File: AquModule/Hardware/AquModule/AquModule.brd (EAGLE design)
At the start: 160 x 100 mm, 1 part

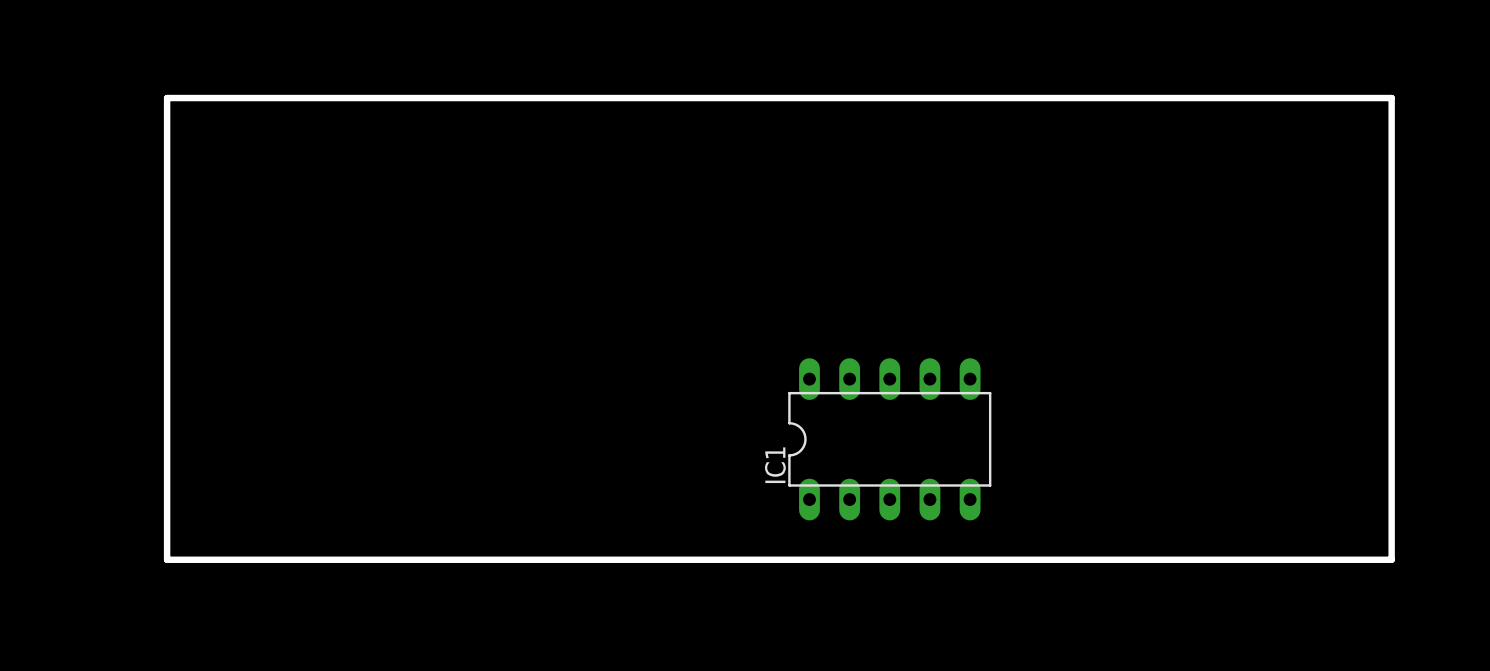
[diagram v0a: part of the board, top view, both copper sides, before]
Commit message: Wired all the components and made first PCB wiring
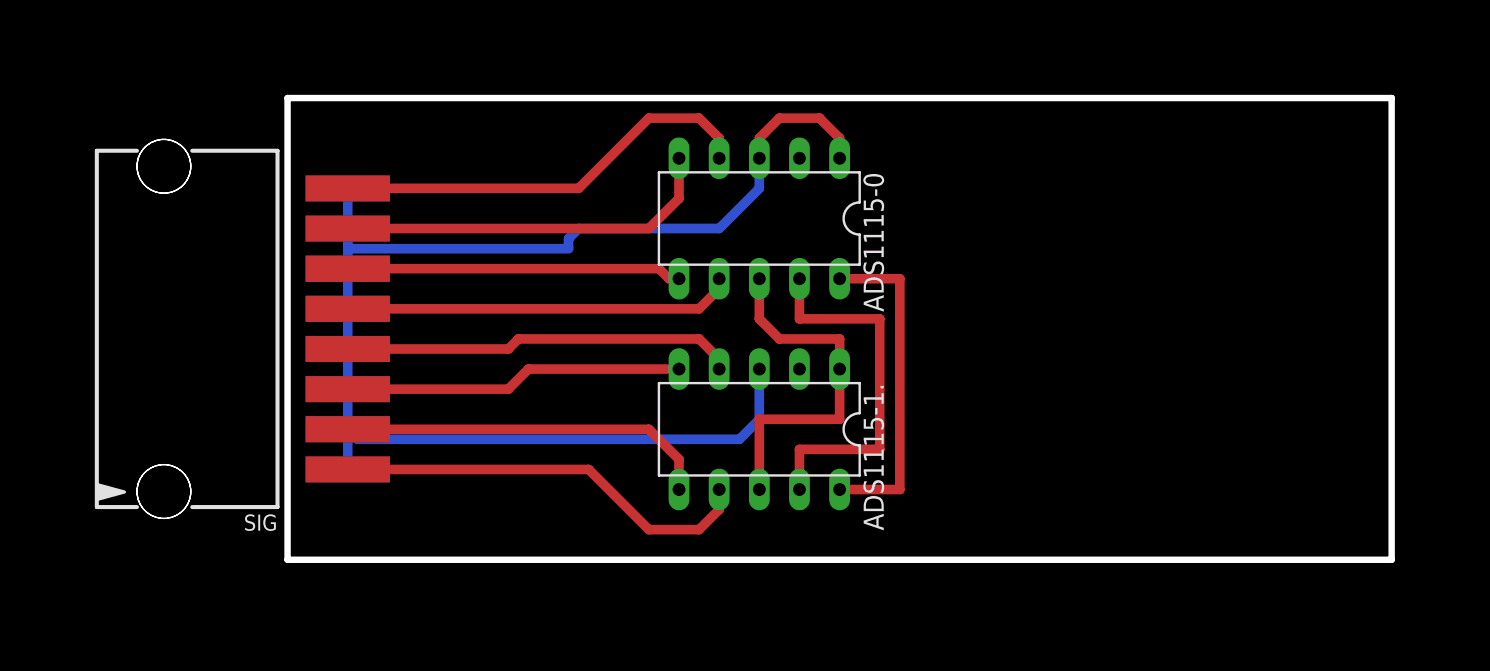
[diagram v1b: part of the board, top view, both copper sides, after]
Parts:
- removed IC1: (no value), ic-package:DIL10
- added ADS1115-0, ADS1115-1.: (no value), ic-package:DIL10
- added GND: GND, con-molex:15-91-08
- added SIG: SIG, con-molex:15-91-08
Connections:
- new net GND: ADS1115-0.1, ADS1115-0.3, ADS1115-1..3, GND.1, GND.2, GND.3, GND.4, GND.5, GND.6, GND.7, GND.8
- new net N$1: ADS1115-0.4, SIG.8
- new net N$2: ADS1115-0.5, SIG.7
- new net N$3: ADS1115-0.6, SIG.6
- new net N$4: ADS1115-0.7, SIG.5
- new net N$5: ADS1115-1..4, SIG.4
- new net N$6: ADS1115-1..5, SIG.3
- new net N$7: ADS1115-1..6, SIG.2
- new net N$8: ADS1115-1..7, SIG.1
- new net SCL: ADS1115-0.10, ADS1115-1..10
- new net SDA: ADS1115-0.9, ADS1115-1..9
- new net VCC: ADS1115-0.8, ADS1115-1..1, ADS1115-1..8
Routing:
- net GND: track 0.00 -> 86.3 mm
- net N$1: track 0.00 -> 27.1 mm
- net N$8: track 0.00 -> 26.9 mm
- net N$5: track 0.00 -> 24.9 mm
- net N$4: track 0.00 -> 24.7 mm
- net N$2: track 0.00 -> 24.3 mm
- net N$7: track 0.00 -> 23.6 mm
- net SDA: track 0.00 -> 23.5 mm
- net VCC: track 0.00 -> 22.8 mm
- net N$6: track 0.00 -> 21.5 mm
- net N$3: track 0.00 -> 21.2 mm
- net SCL: track 0.00 -> 21.0 mm
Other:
- outline, holes or cut-outs redrawn
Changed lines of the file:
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@@
 <setting verticaltext="up"/>
 </settings>
-<grid distance="0.05" unitdist="inch" unit="mm" style="dots" multiple="1" display="yes" altdistance="0.025" altunitdist="inch" altunit="inch"/>
+<grid distance="0.635" unitdist="mm" unit="mm" style="dots" multiple="1" display="yes" altdistance="0.025" altunitdist="inch" altunit="inch"/>
 <layers>
 <layer number="1" name="Top" color="4" fill="1" visible="yes" active="yes"/>
@@
 <dimension x1="38.1" y1="71.12" x2="115.57" y2="71.12" x3="76.835" y3="77.47" textsize="1.778" layer="46"/>
 <dimension x1="115.57" y1="71.12" x2="115.57" y2="41.91" x3="121.92" y3="56.515" textsize="1.778" layer="46"/>
-<wire x1="38.1" y1="71.12" x2="115.57" y2="71.12" width="0.4064" layer="46"/>
+<wire x1="45.72" y1="71.12" x2="115.57" y2="71.12" width="0.4064" layer="46"/>
 <wire x1="115.57" y1="71.12" x2="115.57" y2="41.91" width="0.4064" layer="46"/>
-<wire x1="115.57" y1="41.91" x2="38.1" y2="41.91" width="0.4064" layer="46"/>
-<wire x1="38.1" y1="41.91" x2="38.1" y2="71.12" width="0.4064" layer="46"/>
+<wire x1="115.57" y1="41.91" x2="45.72" y2="41.91" width="0.4064" layer="46"/>
+<wire x1="45.72" y1="41.91" x2="45.72" y2="71.12" width="0.4064" layer="46"/>
 </plain>
 <attributes>
@@
 </autorouter>
 <elements>
-<element name="IC1" library="ic-package" package="DIL10" value="" x="83.82" y="49.53"/>
+<element name="ADS1115-1." library="ic-package" package="DIL10" value="" x="75.565" y="50.165" rot="R180"/>
+<element name="SIG" library="con-molex" package="15-91-08" value="SIG" x="38.735" y="56.515" rot="R90">
+<attribute name="OC_NEWARK" value="unknown" x="38.735" y="56.515" size="1.778" layer="27" rot="R90" display="off"/>
+<attribute name="MPN" value="" x="38.735" y="56.515" size="1.778" layer="27" rot="R90" display="off"/>
+<attribute name="MF" value="" x="38.735" y="56.515" size="1.778" layer="27" rot="R90" display="off"/>
+<attribute name="OC_FARNELL" value="unknown" x="38.735" y="56.515" size="1.778" layer="27" rot="R90" display="off"/>
+</element>
+<element name="GND" library="con-molex" package="15-91-08" value="GND" x="38.735" y="56.515" rot="MR270">
+<attribute name="OC_NEWARK" value="unknown" x="38.735" y="56.515" size="1.778" layer="28" rot="MR270" display="off"/>
+<attribute name="MPN" value="" x="38.735" y="56.515" size="1.778" layer="28" rot="MR270" display="off"/>
+<attribute name="MF" value="" x="38.735" y="56.515" size="1.778" layer="28" rot="MR270" display="off"/>
+<attribute name="OC_FARNELL" value="unknown" x="38.735" y="56.515" size="1.778" layer="28" rot="MR270" display="off"/>
+</element>
+<element name="ADS1115-0" library="ic-package" package="DIL10" value="" x="75.565" y="63.5" rot="R180"/>
 </elements>
 <signals>
+<signal name="N$1">
+<contactref element="ADS1115-0" pad="4"/>
+<contactref element="SIG" pad="8"/>
+<wire x1="73.025" y1="67.31" x2="73.025" y2="68.58" width="0.6096" layer="1"/>
+<wire x1="73.025" y1="68.58" x2="71.755" y2="69.85" width="0.6096" layer="1"/>
+<wire x1="71.755" y1="69.85" x2="68.58" y2="69.85" width="0.6096" layer="1"/>
+<wire x1="68.58" y1="69.85" x2="64.135" y2="65.405" width="0.6096" layer="1"/>
+<wire x1="64.135" y1="65.405" x2="49.53" y2="65.405" width="0.6096" layer="1"/>
+</signal>
+<signal name="N$2">
+<contactref element="ADS1115-0" pad="5"/>
+<contactref element="SIG" pad="7"/>
+<wire x1="49.53" y1="62.865" x2="68.58" y2="62.865" width="0.6096" layer="1"/>
+<wire x1="68.58" y1="62.865" x2="70.485" y2="64.77" width="0.6096" layer="1"/>
+<wire x1="70.485" y1="64.77" x2="70.485" y2="67.31" width="0.6096" layer="1"/>
+</signal>
+<signal name="N$3">
+<contactref element="ADS1115-0" pad="6"/>
+<contactref element="SIG" pad="6"/>
+<wire x1="70.485" y1="59.69" x2="69.85" y2="59.69" width="0.6096" layer="1"/>
+<wire x1="69.85" y1="59.69" x2="69.215" y2="60.325" width="0.6096" layer="1"/>
+<wire x1="69.215" y1="60.325" x2="49.53" y2="60.325" width="0.6096" layer="1"/>
+</signal>
+<signal name="N$4">
+<contactref element="ADS1115-0" pad="7"/>
+<contactref element="SIG" pad="5"/>
+<wire x1="49.53" y1="57.785" x2="71.755" y2="57.785" width="0.6096" layer="1"/>
+<wire x1="71.755" y1="57.785" x2="73.025" y2="59.055" width="0.6096" layer="1"/>
+<wire x1="73.025" y1="59.055" x2="73.025" y2="59.69" width="0.6096" layer="1"/>
+</signal>
+<signal name="N$5">
+<contactref element="ADS1115-1." pad="4"/>
+<contactref element="SIG" pad="4"/>
+<wire x1="73.025" y1="53.975" x2="73.025" y2="54.61" width="0.6096" layer="1"/>
+<wire x1="73.025" y1="54.61" x2="71.755" y2="55.88" width="0.6096" layer="1"/>
+<wire x1="71.755" y1="55.88" x2="60.325" y2="55.88" width="0.6096" layer="1"/>
+<wire x1="60.325" y1="55.88" x2="59.69" y2="55.245" width="0.6096" layer="1"/>
+<wire x1="59.69" y1="55.245" x2="49.53" y2="55.245" width="0.6096" layer="1"/>
+</signal>
+<signal name="N$6">
+<contactref element="ADS1115-1." pad="5"/>
+<contactref element="SIG" pad="3"/>
+<wire x1="70.485" y1="53.975" x2="60.96" y2="53.975" width="0.6096" layer="1"/>
+<wire x1="60.96" y1="53.975" x2="59.69" y2="52.705" width="0.6096" layer="1"/>
+<wire x1="59.69" y1="52.705" x2="49.53" y2="52.705" width="0.6096" layer="1"/>
+</signal>
+<signal name="N$7">
+<contactref element="SIG" pad="2"/>
+<wire x1="49.53" y1="50.165" x2="68.58" y2="50.165" width="0.6096" layer="1"/>
+<wire x1="68.58" y1="50.165" x2="70.485" y2="48.26" width="0.6096" layer="1"/>
+<contactref element="ADS1115-1." pad="6"/>
+<wire x1="70.485" y1="48.26" x2="70.485" y2="46.355" width="0.6096" layer="1"/>
+</signal>
+<signal name="N$8">
+<contactref element="ADS1115-1." pad="7"/>
+<contactref element="SIG" pad="1"/>
+<wire x1="73.025" y1="46.355" x2="73.025" y2="45.085" width="0.6096" layer="1"/>
+<wire x1="73.025" y1="45.085" x2="71.755" y2="43.815" width="0.6096" layer="1"/>
+<wire x1="71.755" y1="43.815" x2="68.58" y2="43.815" width="0.6096" layer="1"/>
+<wire x1="68.58" y1="43.815" x2="64.77" y2="47.625" width="0.6096" layer="1"/>
+<wire x1="64.77" y1="47.625" x2="49.53" y2="47.625" width="0.6096" layer="1"/>
+</signal>
+<signal name="GND">
+<contactref element="GND" pad="8"/>
+<contactref element="GND" pad="7"/>
+<contactref element="GND" pad="6"/>
+<contactref element="GND" pad="5"/>
+<contactref element="GND" pad="4"/>
+<contactref element="GND" pad="3"/>
+<contactref element="GND" pad="2"/>
+<contactref element="GND" pad="1"/>
+<contactref element="ADS1115-0" pad="3"/>
+<contactref element="ADS1115-0" pad="1"/>
+<contactref element="ADS1115-1." pad="3"/>
+<wire x1="75.565" y1="67.31" x2="75.565" y2="68.58" width="0.6096" layer="1"/>
+<wire x1="75.565" y1="68.58" x2="76.835" y2="69.85" width="0.6096" layer="1"/>
+<wire x1="76.835" y1="69.85" x2="79.375" y2="69.85" width="0.6096" layer="1"/>
+<wire x1="79.375" y1="69.85" x2="80.645" y2="68.58" width="0.6096" layer="1"/>
+<wire x1="80.645" y1="68.58" x2="80.645" y2="67.31" width="0.6096" layer="1"/>
+<wire x1="75.565" y1="53.975" x2="75.565" y2="50.8" width="0.6096" layer="16"/>
+<wire x1="75.565" y1="50.8" x2="74.295" y2="49.53" width="0.6096" layer="16"/>
+<wire x1="74.295" y1="49.53" x2="50.165" y2="49.53" width="0.6096" layer="16"/>
+<wire x1="50.165" y1="49.53" x2="49.53" y2="50.165" width="0.6096" layer="16"/>
+<wire x1="49.53" y1="47.625" x2="49.53" y2="50.165" width="0.6096" layer="16"/>
+<wire x1="49.53" y1="52.705" x2="49.53" y2="55.245" width="0.6096" layer="16"/>
+<wire x1="49.53" y1="57.785" x2="49.53" y2="55.245" width="0.6096" layer="16"/>
+<wire x1="49.53" y1="52.705" x2="49.53" y2="50.165" width="0.6096" layer="16"/>
+<wire x1="49.53" y1="60.325" x2="49.53" y2="57.785" width="0.6096" layer="16"/>
+<wire x1="49.53" y1="62.865" x2="49.53" y2="61.595" width="0.6096" layer="16"/>
+<wire x1="49.53" y1="61.595" x2="49.53" y2="60.325" width="0.6096" layer="16"/>
+<wire x1="49.53" y1="62.865" x2="49.53" y2="65.405" width="0.6096" layer="16"/>
+<wire x1="75.565" y1="67.31" x2="75.565" y2="65.405" width="0.6096" layer="16"/>
+<wire x1="75.565" y1="65.405" x2="73.025" y2="62.865" width="0.6096" layer="16"/>
+<wire x1="73.025" y1="62.865" x2="64.135" y2="62.865" width="0.6096" layer="16"/>
+<wire x1="64.135" y1="62.865" x2="63.5" y2="62.23" width="0.6096" layer="16"/>
+<wire x1="63.5" y1="62.23" x2="63.5" y2="61.595" width="0.6096" layer="16"/>
+<wire x1="63.5" y1="61.595" x2="49.53" y2="61.595" width="0.6096" layer="16"/>
+</signal>
+<signal name="VCC">
+<contactref element="ADS1115-0" pad="8"/>
+<contactref element="ADS1115-1." pad="8"/>
+<contactref element="ADS1115-1." pad="1"/>
+<wire x1="75.565" y1="46.355" x2="75.565" y2="50.8" width="0.6096" layer="1"/>
+<wire x1="75.565" y1="50.8" x2="80.645" y2="50.8" width="0.6096" layer="1"/>
+<wire x1="80.645" y1="50.8" x2="80.645" y2="53.975" width="0.6096" layer="1"/>
+<wire x1="80.645" y1="53.975" x2="80.645" y2="55.88" width="0.6096" layer="1"/>
+<wire x1="80.645" y1="55.88" x2="76.835" y2="55.88" width="0.6096" layer="1"/>
+<wire x1="76.835" y1="55.88" x2="75.565" y2="57.15" width="0.6096" layer="1"/>
+<wire x1="75.565" y1="57.15" x2="75.565" y2="59.69" width="0.6096" layer="1"/>
+</signal>
+<signal name="SCL">
+<contactref element="ADS1115-0" pad="10"/>
+<contactref element="ADS1115-1." pad="10"/>
+<wire x1="80.645" y1="59.69" x2="84.455" y2="59.69" width="0.6096" layer="1"/>
+<wire x1="84.455" y1="59.69" x2="84.455" y2="46.355" width="0.6096" layer="1"/>
+<wire x1="84.455" y1="46.355" x2="80.645" y2="46.355" width="0.6096" layer="1"/>
+</signal>
+<signal name="SDA">
+<contactref element="ADS1115-0" pad="9"/>
+<contactref element="ADS1115-1." pad="9"/>
+<wire x1="78.105" y1="59.69" x2="78.105" y2="57.15" width="0.6096" layer="1"/>
+<wire x1="78.105" y1="57.15" x2="83.185" y2="57.15" width="0.6096" layer="1"/>
+<wire x1="83.185" y1="57.15" x2="83.185" y2="48.895" width="0.6096" layer="1"/>
+<wire x1="83.185" y1="48.895" x2="78.105" y2="48.895" width="0.6096" layer="1"/>
+<wire x1="78.105" y1="48.895" x2="78.105" y2="46.355" width="0.6096" layer="1"/>
+</signal>
 </signals>
 </board>

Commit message: PCB design for module 1 - Ready
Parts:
- added C1, C2, C3, C4, C5, C6, C7, C8: 100nF, rcl:C1005
- added POW_LED: LS_T679-D2E2-1, led:PLCC2
- added R1, R2, R3, R4, R5, R6, R7, R8: 1K, resistor:R0603
- added R9: ?, resistor:0207/2V
- moved GND 26.7 mm to (14.6, 45.1)
- moved SIG 26.7 mm to (14.6, 45.1)
- moved ADS1115-0 21.5 mm to (57.8, 51.4)
- moved ADS1115-1. 21.1 mm to (57.8, 38.7)
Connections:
- new net N$10: R2.1, SIG.7
- new net N$11: R3.1, SIG.6
- new net N$12: R4.1, SIG.5
- new net N$13: R5.1, SIG.4
- new net N$14: R6.1, SIG.3
- new net N$15: R7.1, SIG.2
- new net N$16: R8.1, SIG.1
- new net N$17: POW_LED.C, R9.2
- new net N$9: R1.1, SIG.8
- net GND: now also C1.1, C2.1, C3.1, C4.1, C5.1, C6.1, C7.1, C8.1, R9.1
- net N$1: now also C8.2, R1.2; no longer SIG.8
- net N$2: now also C7.2, R2.2; no longer SIG.7
- net N$3: now also C6.2, R3.2; no longer SIG.6
- net N$4: now also C5.2, R4.2; no longer SIG.5
- net N$5: now also C4.2, R5.2; no longer SIG.4
- net N$6: now also C3.2, R6.2; no longer SIG.3
- net N$7: now also C2.2, R7.2; no longer SIG.2
- net N$8: now also C1.2, R8.2; no longer SIG.1
- net VCC: now also POW_LED.A
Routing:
- net GND: track 86.3 -> 0.00 mm
- net VCC: track 22.8 -> 36.6 mm, vias 0 -> 1
- net N$9: track 0.00 -> 7.41 mm
- net N$16: track 0.00 -> 7.41 mm
- net N$15: track 0.00 -> 7.41 mm
- net N$14: track 0.00 -> 7.41 mm
- net N$13: track 0.00 -> 7.41 mm
- net N$12: track 0.00 -> 7.41 mm
- net N$11: track 0.00 -> 7.41 mm
- net N$10: track 0.00 -> 7.41 mm
- net SCL: track 21.0 -> 26.6 mm
- net N$17: track 0.00 -> 4.02 mm
- net SDA: track 23.5 -> 27.1 mm
- net N$7: track 23.6 -> 20.9 mm
- net N$1: track 27.1 -> 29.1 mm, vias 0 -> 1
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- added copper zone on layer 16, net GND
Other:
- board size 160 x 100 mm -> 100 x 80 mm
